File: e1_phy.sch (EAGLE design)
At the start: 134 parts, among them IC2 LD117AS33TR, IC3 LD117AS33TR, U1 IDT82V2081, U2 GPS_GNS_2201, U3 VCTCXO-CONNORWINFIELD, U4 VCXO_TAITIEN_VT, U5 IP4234CZ6, U7 IP4234CZ6, X1 BU-SMA-G, X3 JACK2.5_SJ-2523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

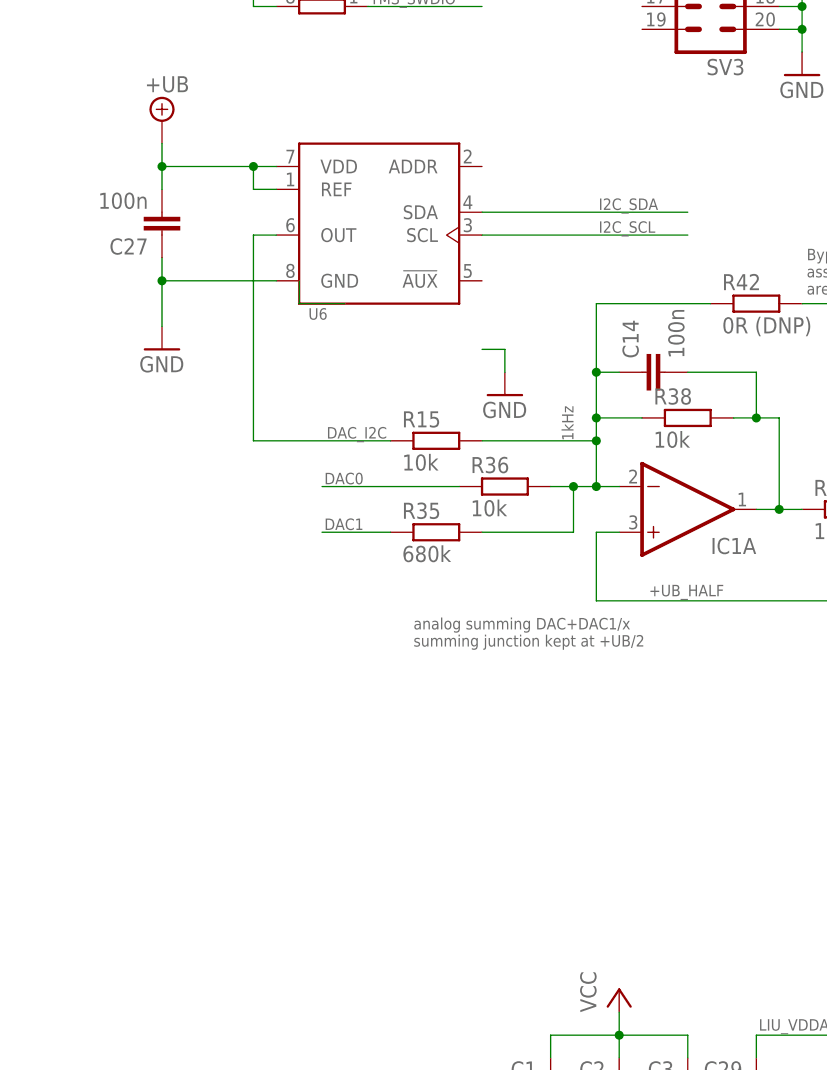
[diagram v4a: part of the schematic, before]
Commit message: Add footprint for voltage reference, can be bypassed.
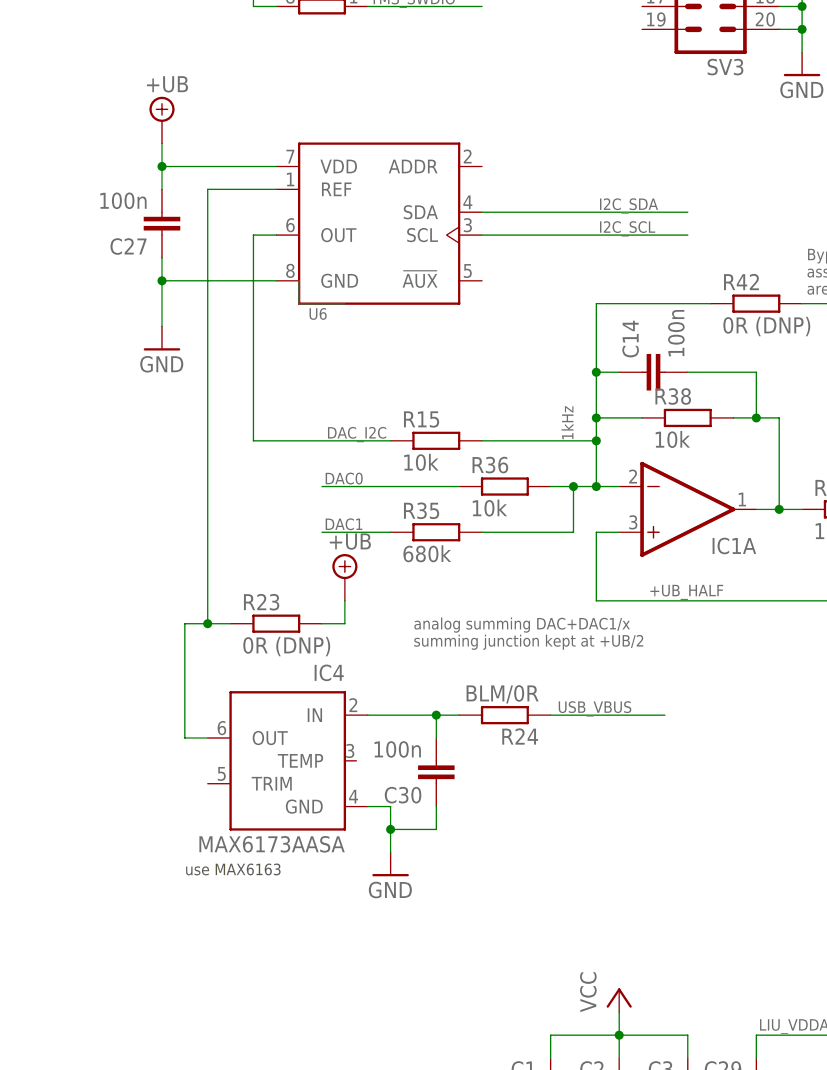
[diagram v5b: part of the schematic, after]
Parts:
- added C30: 100n, rcl:C-EUC0603
- added IC4: MAX6173AASA, maxim:MAX6173AASA
- added R23: 0R (DNP), rcl:R-EU_R0603
- added R24: BLM/0R, rcl:R-EU_R0603
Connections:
- new net N$7: IC4.OUT, R23.1, U6.REF
- new net N$9: C30.2, IC4.IN, R24.2
- net +UB: now also R23.2; no longer U6.REF
- net GND: now also C30.1, IC4.GND
- net USB_VBUS: now also R24.1
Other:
- note added: "use MAX6163"
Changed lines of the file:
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@@
 <part name="GND34" library="supply1" library_urn="urn:adsk.eagle:library:371" deviceset="GND" device=""/>
 <part name="R15" library="rcl" library_urn="urn:adsk.eagle:library:334" deviceset="R-EU_" device="R0603" package3d_urn="urn:adsk.eagle:package:23555/2" value="10k"/>
-<part name="GND35" library="supply1" library_urn="urn:adsk.eagle:library:371" deviceset="GND" device=""/>
 <part name="C28" library="rcl" library_urn="urn:adsk.eagle:library:334" deviceset="C-EU" device="C0603" package3d_urn="urn:adsk.eagle:package:23616/2" value="100n"/>
 <part name="GND36" library="supply1" library_urn="urn:adsk.eagle:library:371" deviceset="GND" device=""/>
@@
 <part name="R22" library="rcl" library_urn="urn:adsk.eagle:library:334" deviceset="R-EU_" device="R0603" package3d_urn="urn:adsk.eagle:package:23555/2" value="33R"/>
 <part name="X1" library="con-coax" library_urn="urn:adsk.eagle:library:133" deviceset="BU-SMA-G" device="" package3d_urn="urn:adsk.eagle:package:6205/1"/>
+<part name="IC4" library="maxim" library_urn="urn:adsk.eagle:library:269" deviceset="MAX617*ASA" device="" package3d_urn="urn:adsk.eagle:package:17511/1" technology="3A"/>
+<part name="R23" library="rcl" library_urn="urn:adsk.eagle:library:334" deviceset="R-EU_" device="R0603" package3d_urn="urn:adsk.eagle:package:23555/2" value="0R (DNP)"/>
+<part name="GND16" library="supply1" library_urn="urn:adsk.eagle:library:371" deviceset="GND" device=""/>
+<part name="SUPPLY9" library="supply2" library_urn="urn:adsk.eagle:library:372" deviceset="+UB" device=""/>
+<part name="C30" library="rcl" library_urn="urn:adsk.eagle:library:334" deviceset="C-EU" device="C0603" package3d_urn="urn:adsk.eagle:package:23616/2" value="100n"/>
+<part name="R24" library="rcl" library_urn="urn:adsk.eagle:library:334" deviceset="R-EU_" device="R0603" package3d_urn="urn:adsk.eagle:package:23555/2" value="BLM/0R"/>
 </parts>
 <sheets>
@@
 4="TxD"=#CS2</text>
 <text x="15.24" y="200.66" size="1.778" layer="97">Power LEDs</text>
+<text x="208.28" y="134.62" size="1.27" layer="97">use MAX6163</text>
 </plain>
 <instances>
@@
 <instance part="GND34" gate="1" x="205.74" y="193.04"/>
 <instance part="R15" gate="G$1" x="236.22" y="182.88"/>
-<instance part="GND35" gate="1" x="243.84" y="187.96"/>
 <instance part="C28" gate="G$1" x="358.14" y="152.4" rot="MR90"/>
 <instance part="GND36" gate="1" x="363.22" y="147.32"/>
@@
 <instance part="R22" gate="G$1" x="353.06" y="218.44"/>
 <instance part="X1" gate="G1" x="284.48" y="251.46"/>
+<instance part="IC4" gate="G$1" x="220.98" y="147.32" rot="MR0"/>
+<instance part="R23" gate="G$1" x="218.44" y="162.56"/>
+<instance part="GND16" gate="1" x="231.14" y="134.62"/>
+<instance part="SUPPLY9" gate="G$1" x="226.06" y="167.64"/>
+<instance part="C30" gate="G$1" x="236.22" y="144.78" rot="R180"/>
+<instance part="R24" gate="G$1" x="243.84" y="152.4" rot="R180"/>
 </instances>
 <busses>
@@
 <wire x1="218.44" y1="200.66" x2="205.74" y2="200.66" width="0.1524" layer="91"/>
 <junction x="205.74" y="200.66"/>
-</segment>
-<segment>
-<wire x1="241.3" y1="193.04" x2="243.84" y2="193.04" width="0.1524" layer="91"/>
-<wire x1="243.84" y1="193.04" x2="243.84" y2="190.5" width="0.1524" layer="91"/>
-<pinref part="GND35" gate="1" pin="GND"/>
 </segment>
 <segment>
@@
 <pinref part="GND15" gate="1" pin="GND"/>
 </segment>
+<segment>
+<pinref part="IC4" gate="G$1" pin="GND"/>
+<wire x1="228.6" y1="142.24" x2="231.14" y2="142.24" width="0.1524" layer="91"/>
+<pinref part="GND16" gate="1" pin="GND"/>
+<wire x1="231.14" y1="142.24" x2="231.14" y2="139.7" width="0.1524" layer="91"/>
+<wire x1="231.14" y1="139.7" x2="231.14" y2="137.16" width="0.1524" layer="91"/>
+<wire x1="231.14" y1="139.7" x2="236.22" y2="139.7" width="0.1524" layer="91"/>
+<junction x="231.14" y="139.7"/>
+<pinref part="C30" gate="G$1" pin="1"/>
+<wire x1="236.22" y1="139.7" x2="236.22" y2="142.24" width="0.1524" layer="91"/>
+</segment>
 </net>
 <net name="LINE_PIN1" class="0">
@@
 <label x="73.66" y="256.54" size="1.778" layer="95"/>
 </segment>
+<segment>
+<pinref part="R24" gate="G$1" pin="1"/>
+<wire x1="248.92" y1="152.4" x2="261.62" y2="152.4" width="0.1524" layer="91"/>
+<label x="249.682" y="152.654" size="1.27" layer="95"/>
+</segment>
 </net>
 <net name="USB_DDM_CON" class="0">
@@
 <pinref part="U6" gate="G$1" pin="VDD"/>
 <wire x1="205.74" y1="213.36" x2="205.74" y2="210.82" width="0.1524" layer="91"/>
-<wire x1="218.44" y1="213.36" x2="215.9" y2="213.36" width="0.1524" layer="91"/>
 <junction x="205.74" y="213.36"/>
-<pinref part="U6" gate="G$1" pin="REF"/>
-<wire x1="215.9" y1="213.36" x2="205.74" y2="213.36" width="0.1524" layer="91"/>
-<wire x1="218.44" y1="210.82" x2="215.9" y2="210.82" width="0.1524" layer="91"/>
-<wire x1="215.9" y1="210.82" x2="215.9" y2="213.36" width="0.1524" layer="91"/>
-<junction x="215.9" y="213.36"/>
+<wire x1="218.44" y1="213.36" x2="205.74" y2="213.36" width="0.1524" layer="91"/>
 </segment>
 <segment>
@@
 <pinref part="SUPPLY8" gate="G$1" pin="+UB"/>
 <wire x1="350.52" y1="116.84" x2="350.52" y2="114.3" width="0.1524" layer="91"/>
+</segment>
+<segment>
+<pinref part="SUPPLY9" gate="G$1" pin="+UB"/>
+<wire x1="226.06" y1="165.1" x2="226.06" y2="162.56" width="0.1524" layer="91"/>
+<pinref part="R23" gate="G$1" pin="2"/>
+<wire x1="223.52" y1="162.56" x2="226.06" y2="162.56" width="0.1524" layer="91"/>
 </segment>
 </net>
@@
 </segment>
 </net>
+<net name="N$7" class="0">
+<segment>
+<pinref part="IC4" gate="G$1" pin="OUT"/>
+<wire x1="210.82" y1="149.86" x2="208.28" y2="149.86" width="0.1524" layer="91"/>
+<wire x1="208.28" y1="149.86" x2="208.28" y2="162.56" width="0.1524" layer="91"/>
+<pinref part="R23" gate="G$1" pin="1"/>
+<wire x1="208.28" y1="162.56" x2="210.82" y2="162.56" width="0.1524" layer="91"/>
+<pinref part="U6" gate="G$1" pin="REF"/>
+<wire x1="210.82" y1="162.56" x2="213.36" y2="162.56" width="0.1524" layer="91"/>
+<wire x1="218.44" y1="210.82" x2="210.82" y2="210.82" width="0.1524" layer="91"/>
+<wire x1="210.82" y1="210.82" x2="210.82" y2="162.56" width="0.1524" layer="91"/>
+<junction x="210.82" y="162.56"/>
+</segment>
+</net>
+<net name="N$9" class="0">
+<segment>
+<pinref part="IC4" gate="G$1" pin="IN"/>
+<wire x1="228.6" y1="152.4" x2="236.22" y2="152.4" width="0.1524" layer="91"/>
+<pinref part="C30" gate="G$1" pin="2"/>
+<wire x1="236.22" y1="152.4" x2="236.22" y2="149.86" width="0.1524" layer="91"/>
+<pinref part="R24" gate="G$1" pin="2"/>
+<wire x1="236.22" y1="152.4" x2="238.76" y2="152.4" width="0.1524" layer="91"/>
+<junction x="236.22" y="152.4"/>
+</segment>
+</net>

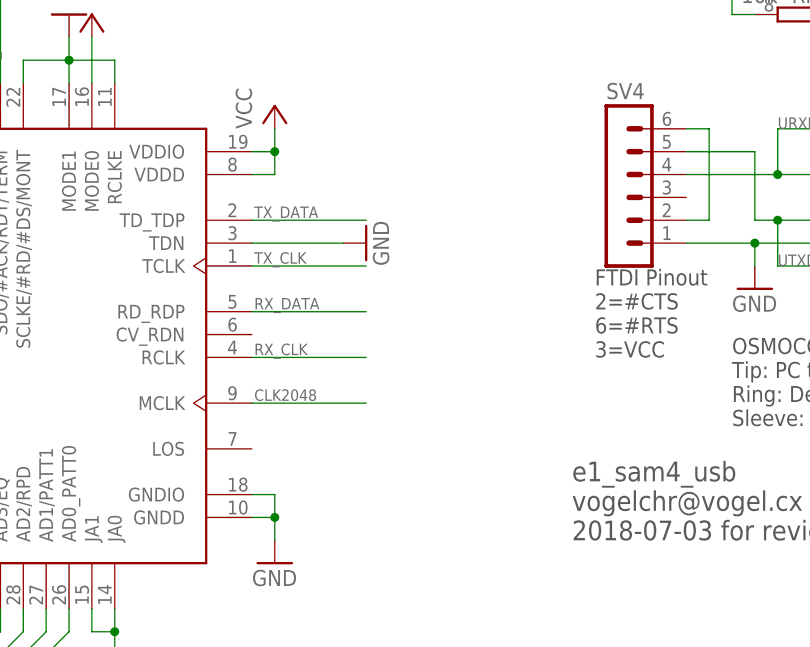
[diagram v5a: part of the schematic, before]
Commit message: Testpads for unused LIU signals.
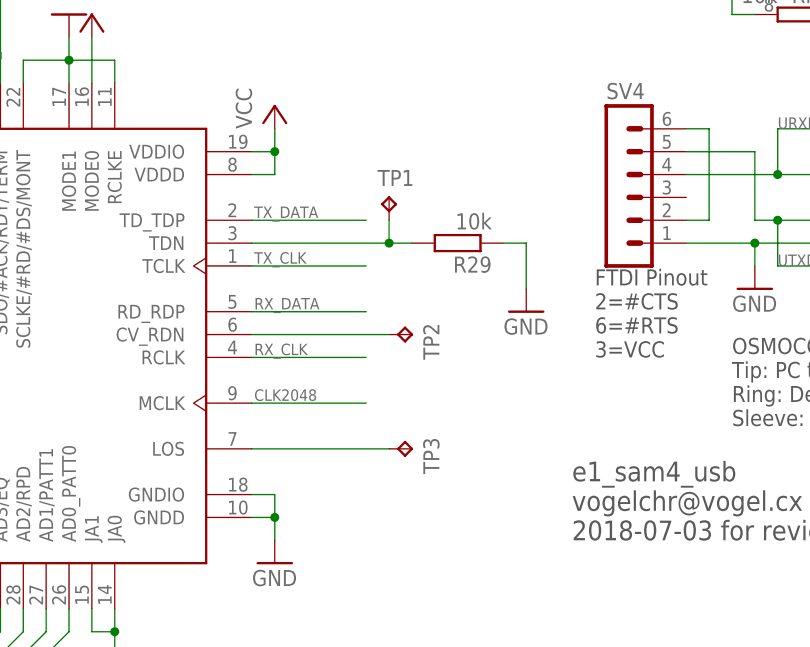
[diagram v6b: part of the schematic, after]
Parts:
- added R29: 10k, rcl:R-EU_R0603
- added TP1, TP2, TP3: TPB1,27, testpad:TPB1,27
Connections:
- new net N$4: TP2.TP, U1.CV_RDN
- new net N$6: R29.2, TP1.TP, U1.TDN
- new net N$8: TP3.TP, U1.LOS
- net GND: now also R29.1; no longer U1.TDN
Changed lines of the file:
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@@
 <part name="C30" library="rcl" library_urn="urn:adsk.eagle:library:334" deviceset="C-EU" device="C0603" package3d_urn="urn:adsk.eagle:package:23616/2" value="100n"/>
 <part name="R24" library="rcl" library_urn="urn:adsk.eagle:library:334" deviceset="R-EU_" device="R0603" package3d_urn="urn:adsk.eagle:package:23555/2" value="BLM/0R"/>
+<part name="TP1" library="testpad" library_urn="urn:adsk.eagle:library:385" deviceset="TP" device="B1,27" package3d_urn="urn:adsk.eagle:package:27944/1"/>
+<part name="TP2" library="testpad" library_urn="urn:adsk.eagle:library:385" deviceset="TP" device="B1,27" package3d_urn="urn:adsk.eagle:package:27944/1"/>
+<part name="R29" library="rcl" library_urn="urn:adsk.eagle:library:334" deviceset="R-EU_" device="R0603" package3d_urn="urn:adsk.eagle:package:23555/2" value="10k"/>
+<part name="TP3" library="testpad" library_urn="urn:adsk.eagle:library:385" deviceset="TP" device="B1,27" package3d_urn="urn:adsk.eagle:package:27944/1"/>
 </parts>
 <sheets>
@@
 <attribute name="VALUE" x="236.22" y="86.36" size="1.778" layer="96" rot="R90"/>
 </instance>
-<instance part="GND7" gate="1" x="266.7" y="58.42" smashed="yes" rot="R90">
-<attribute name="VALUE" x="269.24" y="55.88" size="1.778" layer="96" rot="R90"/>
+<instance part="GND7" gate="1" x="284.48" y="50.8" smashed="yes">
+<attribute name="VALUE" x="281.94" y="48.26" size="1.778" layer="96"/>
 </instance>
 <instance part="GND8" gate="1" x="238.76" y="10.16"/>
@@
 <instance part="C30" gate="G$1" x="236.22" y="144.78" rot="R180"/>
 <instance part="R24" gate="G$1" x="243.84" y="152.4" rot="R180"/>
+<instance part="TP1" gate="G$1" x="269.24" y="63.5"/>
+<instance part="TP2" gate="G$1" x="271.78" y="48.26" rot="R270"/>
+<instance part="R29" gate="G$1" x="276.86" y="58.42" rot="R180"/>
+<instance part="TP3" gate="G$1" x="271.78" y="35.56" rot="R270"/>
 </instances>
 <busses>
@@
 <wire x1="228.6" y1="76.2" x2="228.6" y2="78.74" width="0.1524" layer="91"/>
 <wire x1="228.6" y1="78.74" x2="233.68" y2="78.74" width="0.1524" layer="91"/>
-</segment>
-<segment>
-<pinref part="GND7" gate="1" pin="GND"/>
-<pinref part="U1" gate="G$1" pin="TDN"/>
-<wire x1="264.16" y1="58.42" x2="254" y2="58.42" width="0.1524" layer="91"/>
 </segment>
 <segment>
@@
 <wire x1="236.22" y1="139.7" x2="236.22" y2="142.24" width="0.1524" layer="91"/>
 </segment>
+<segment>
+<pinref part="R29" gate="G$1" pin="1"/>
+<wire x1="281.94" y1="58.42" x2="284.48" y2="58.42" width="0.1524" layer="91"/>
+<pinref part="GND7" gate="1" pin="GND"/>
+<wire x1="284.48" y1="58.42" x2="284.48" y2="53.34" width="0.1524" layer="91"/>
+</segment>
 </net>
 <net name="LINE_PIN1" class="0">
@@
 </segment>
 </net>
+<net name="N$4" class="0">
+<segment>
+<pinref part="U1" gate="G$1" pin="CV_RDN"/>
+<pinref part="TP2" gate="G$1" pin="TP"/>
+<wire x1="254" y1="48.26" x2="269.24" y2="48.26" width="0.1524" layer="91"/>
+</segment>
+</net>
+<net name="N$6" class="0">
+<segment>
+<pinref part="U1" gate="G$1" pin="TDN"/>
+<pinref part="R29" gate="G$1" pin="2"/>
+<wire x1="254" y1="58.42" x2="269.24" y2="58.42" width="0.1524" layer="91"/>
+<pinref part="TP1" gate="G$1" pin="TP"/>
+<wire x1="269.24" y1="58.42" x2="271.78" y2="58.42" width="0.1524" layer="91"/>
+<wire x1="269.24" y1="60.96" x2="269.24" y2="58.42" width="0.1524" layer="91"/>
+<junction x="269.24" y="58.42"/>
+</segment>
+</net>
+<net name="N$8" class="0">
+<segment>
+<pinref part="U1" gate="G$1" pin="LOS"/>
+<pinref part="TP3" gate="G$1" pin="TP"/>
+<wire x1="254" y1="35.56" x2="269.24" y2="35.56" width="0.1524" layer="91"/>
+</segment>
+</net>

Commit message: Cleaned up silkscreen.
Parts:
- added TP4, TP5, TP6: TPB1,27, testpad:TPB1,27
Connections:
- net CLK2048: now also TP4.TP
- net N$7: now also TP6.TP
- net TX_CLK: now also TP5.TP
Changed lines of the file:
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@@
 <part name="R29" library="rcl" library_urn="urn:adsk.eagle:library:334" deviceset="R-EU_" device="R0603" package3d_urn="urn:adsk.eagle:package:23555/2" value="10k"/>
 <part name="TP3" library="testpad" library_urn="urn:adsk.eagle:library:385" deviceset="TP" device="B1,27" package3d_urn="urn:adsk.eagle:package:27944/1"/>
+<part name="TP4" library="testpad" library_urn="urn:adsk.eagle:library:385" deviceset="TP" device="B1,27" package3d_urn="urn:adsk.eagle:package:27944/1"/>
+<part name="TP5" library="testpad" library_urn="urn:adsk.eagle:library:385" deviceset="TP" device="B1,27" package3d_urn="urn:adsk.eagle:package:27944/1"/>
+<part name="TP6" library="testpad" library_urn="urn:adsk.eagle:library:385" deviceset="TP" device="B1,27" package3d_urn="urn:adsk.eagle:package:27944/1"/>
 </parts>
 <sheets>
@@
 <instance part="R29" gate="G$1" x="276.86" y="58.42" rot="R180"/>
 <instance part="TP3" gate="G$1" x="271.78" y="35.56" rot="R270"/>
+<instance part="TP4" gate="G$1" x="276.86" y="45.72"/>
+<instance part="TP5" gate="G$1" x="269.24" y="55.88" rot="R270"/>
+<instance part="TP6" gate="G$1" x="208.28" y="167.64"/>
 </instances>
 <busses>
@@
 <segment>
 <pinref part="U1" gate="G$1" pin="MCLK"/>
-<wire x1="254" y1="40.64" x2="266.7" y2="40.64" width="0.1524" layer="91"/>
-<label x="254.254" y="40.894" size="1.27" layer="95"/>
+<label x="277.114" y="40.894" size="1.27" layer="95"/>
+<wire x1="254" y1="40.64" x2="276.86" y2="40.64" width="0.1524" layer="91"/>
+<pinref part="TP4" gate="G$1" pin="TP"/>
+<wire x1="276.86" y1="40.64" x2="284.48" y2="40.64" width="0.1524" layer="91"/>
+<wire x1="276.86" y1="43.18" x2="276.86" y2="40.64" width="0.1524" layer="91"/>
+<junction x="276.86" y="40.64"/>
 </segment>
 </net>
@@
 <wire x1="254" y1="55.88" x2="266.7" y2="55.88" width="0.1524" layer="91"/>
 <label x="254.254" y="56.134" size="1.27" layer="95"/>
+<pinref part="TP5" gate="G$1" pin="TP"/>
 </segment>
 <segment>
@@
 <wire x1="210.82" y1="210.82" x2="210.82" y2="162.56" width="0.1524" layer="91"/>
 <junction x="210.82" y="162.56"/>
-</segment>
-</net>
+<pinref part="TP6" gate="G$1" pin="TP"/>
+<wire x1="208.28" y1="165.1" x2="208.28" y2="162.56" width="0.1524" layer="91"/>
+<junction x="208.28" y="162.56"/>
+</segment>
+</net>
